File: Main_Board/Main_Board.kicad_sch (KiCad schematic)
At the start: 51 parts, among them J1 RJ45_LED_Shielded, J2 Conn_01x12, SW1 SW_Push, SW2 SW_Push, SW3 SW_Push, SW4 SW_Push, SW5 SW_Push, SW6 SW_Push, SW7 SW_Push, SW8 SW_Push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

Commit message: Overviewed the Board with Drew
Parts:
- added BLUE: D, symbol Device:D
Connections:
- net +3V3: now also BLUE.1 (K); no longer C2.1, C3.1, U1.3 (OUT)
- net GND: no longer U6.5
- new net: BLUE.2 (A), C2.1, C3.1, U1.3 (OUT)
- no-connect marks 62 -> 66
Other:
- moved on the sheet: J2
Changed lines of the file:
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@@
 	)
 	(junction
-		(at 107.95 46.99)
-		(diameter 0)
-		(color 0 0 0 0)
-	)
-	(junction
 		(at 194.31 95.25)
 		(diameter 0)
@@
 	)
 	(junction
+		(at 107.95 46.99)
+		(diameter 0)
+		(color 0 0 0 0)
+	)
+	(junction
 		(at 304.8 171.45)
 		(diameter 0)
@@
 	)
 	(no_connect
+		(at 341.63 34.29)
+	)
+	(no_connect
 		(at 97.79 147.32)
 	)
@@
 	)
 	(no_connect
+		(at 341.63 39.37)
+	)
+	(no_connect
 		(at 341.63 113.03)
 	)
@@
 	)
 	(no_connect
+		(at 341.63 128.27)
+	)
+	(no_connect
 		(at 97.79 157.48)
 	)
@@
 	)
 	(no_connect
+		(at 341.63 36.83)
+	)
+	(no_connect
 		(at 341.63 100.33)
 	)
@@
 	(wire
 		(pts
-			(xy 88.9 127) (xy 83.82 127)
-		)
-		(stroke
-			(width 0)
-			(type default)
-		)
-	)
-	(wire
-		(pts
 			(xy 217.17 195.58) (xy 217.17 186.69)
 		)
@@
 	(wire
 		(pts
-			(xy 107.95 44.45) (xy 107.95 46.99)
-		)
-		(stroke
-			(width 0)
-			(type default)
-		)
-	)
-	(wire
-		(pts
 			(xy 80.01 54.61) (xy 93.98 54.61)
 		)
@@
 	(wire
 		(pts
-			(xy 33.02 93.98) (xy 33.02 101.6)
+			(xy 53.34 99.06) (xy 53.34 101.6)
 		)
 		(stroke
@@
 		)
 	)
-	(wire
-		(pts
-			(xy 33.02 101.6) (xy 53.34 101.6)
-		)
-		(stroke
-			(width 0)
-			(type default)
-		)
-	)
 	(polyline
 		(pts
@@
 		)
 	)
+	(wire
+		(pts
+			(xy 97.79 44.45) (xy 100.33 44.45)
+		)
+		(stroke
+			(width 0)
+			(type default)
+		)
+	)
 	(polyline
 		(pts
@@
 	(wire
 		(pts
+			(xy 97.79 44.45) (xy 97.79 43.18)
+		)
+		(stroke
+			(width 0)
+			(type default)
+		)
+	)
+	(wire
+		(pts
 			(xy 217.17 144.78) (xy 220.98 144.78)
 		)
@@
 		)
 	)
-	(wire
-		(pts
-			(xy 83.82 138.43) (xy 53.34 138.43)
-		)
-		(stroke
-			(width 0)
-			(type default)
-		)
-	)
 	(polyline
 		(pts
@@
 	(wire
 		(pts
-			(xy 83.82 127) (xy 83.82 138.43)
-		)
-		(stroke
-			(width 0)
-			(type default)
-		)
-	)
-	(wire
-		(pts
 			(xy 209.55 60.96) (xy 217.17 60.96)
 		)
@@
 	(wire
 		(pts
+			(xy 107.95 44.45) (xy 107.95 46.99)
+		)
+		(stroke
+			(width 0)
+			(type default)
+		)
+	)
+	(wire
+		(pts
 			(xy 173.99 53.34) (xy 175.26 53.34)
 		)
@@
 	(symbol
 		(lib_id "Connector_Generic:Conn_01x12")
-		(at 610.87 35.56 0)
+		(at 379.73 35.56 0)
 		(unit 1)
 		(exclude_from_sim no)
@@
 		(fields_autoplaced yes)
 		(property "Reference" "J2"
-			(at 613.41 35.5599 0)
+			(at 382.27 35.5599 0)
 			(effects
 				(font
@@
 		)
 		(property "Value" "Conn_01x12"
-			(at 613.41 38.0999 0)
+			(at 382.27 38.0999 0)
 			(effects
 				(font
@@
 		)
 		(property "Footprint" ""
-			(at 610.87 35.56 0)
+			(at 379.73 35.56 0)
 			(effects
 				(font
@@
 		)
 		(property "Datasheet" "~"
-			(at 610.87 35.56 0)
+			(at 379.73 35.56 0)
 			(effects
 				(font
@@
 		)
 		(property "Description" "Generic connector, single row, 01x12, script generated (kicad-library-utils/schlib/autogen/connector/)"
-			(at 610.87 35.56 0)
+			(at 379.73 35.56 0)
 			(effects
 				(font
@@
 	(symbol
 		(lib_id "power:+3.3V")
-		(at 107.95 44.45 0)
+		(at 97.79 43.18 0)
 		(unit 1)
 		(exclude_from_sim no)
@@
 		(dnp no)
 		(property "Reference" "#PWR03"
-			(at 107.95 48.26 0)
+			(at 97.79 46.99 0)
 			(effects
 				(font
@@
 		)
 		(property "Value" "+3V3"
-			(at 104.648 39.624 0)
+			(at 94.488 38.354 0)
 			(effects
 				(font
@@
 		)
 		(property "Footprint" ""
-			(at 107.95 44.45 0)
+			(at 97.79 43.18 0)
 			(effects
 				(font
@@
 		)
 		(property "Datasheet" ""
-			(at 107.95 44.45 0)
+			(at 97.79 43.18 0)
 			(effects
 				(font
@@
 		)
 		(property "Description" "Power symbol creates a global label with name \"+3.3V\""
-			(at 107.95 44.45 0)
+			(at 97.79 43.18 0)
 			(effects
 				(font
@@
 	(symbol
 		(lib_id "power:+3V3")
-		(at 33.02 93.98 0)
+		(at 53.34 99.06 0)
 		(unit 1)
 		(exclude_from_sim no)
@@
 		(fields_autoplaced yes)
 		(property "Reference" "#PWR029"
-			(at 33.02 97.79 0)
+			(at 53.34 102.87 0)
 			(effects
 				(font
@@
 		)
 		(property "Value" "+3V3"
-			(at 33.02 90.4042 0)
+			(at 53.34 95.4842 0)
 			(effects
 				(font
@@
 		)
 		(property "Footprint" ""
-			(at 33.02 93.98 0)
+			(at 53.34 99.06 0)
 			(effects
 				(font
@@
 		)
 		(property "Datasheet" ""
-			(at 33.02 93.98 0)
+			(at 53.34 99.06 0)
 			(effects
 				(font
@@
 		)
 		(property "Description" ""
-			(at 33.02 93.98 0)
+			(at 53.34 99.06 0)
 			(effects
 				(font
@@
 					(unit 1)
 				)
+			)
+		)
+	)
+	(symbol
+		(lib_id "Device:D")
+		(at 104.14 44.45 0)
+		(unit 1)
+		(exclude_from_sim no)
+		(in_bom yes)
+		(on_board yes)
+		(dnp no)
+		(property "Reference" "BLUE"
+			(at 104.14 38.1 0)
+			(effects
+				(font
+					(size 1.27 1.27)
+				)
+			)
+		)
+		(property "Value" "D"
+			(at 104.14 40.64 0)
+			(effects
+				(font
+					(size 1.27 1.27)
+				)
+			)
+		)
+		(property "Footprint" ""
+			(at 104.14 44.45 0)
+			(effects
+				(font
+					(size 1.27 1.27)
+				)
+				(hide yes)
+			)
+		)
+		(property "Datasheet" "~"
+			(at 104.14 44.45 0)
+			(effects
+				(font
+					(size 1.27 1.27)
+				)
+				(hide yes)
+			)
+		)
+		(property "Description" "Diode"
+			(at 104.14 44.45 0)
+			(effects
+				(font
+					(size 1.27 1.27)
+				)
+				(hide yes)
+			)
+		)
+		(property "Sim.Device" "D"
+			(at 104.14 44.45 0)
+			(effects
+				(font
+					(size 1.27 1.27)
+				)
+				(hide yes)
+			)
+		)
+		(property "Sim.Pins" "1=K 2=A"
+			(at 104.14 44.45 0)
+			(effects
+				(font
+					(size 1.27 1.27)
+				)
+				(hide yes)
+			)
+		)
+		(pin "2"
+		)
+		(pin "1"
+		)
+		(instances
+			(project ""
+				(path "/7e76cf6a-e9a4-4ef3-bf05-f0b14a5efcef"
+					(reference "BLUE")
+					(unit 1)
+				)

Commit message: Final edit of the schematic is done
Buttons might change depending on testing results.

Next step:
Test the button system with Drew at the e-lab.
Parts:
- removed BLUE: D, symbol Device:D
- removed D2, D3, D4, D5, D6, D7, D8, D9: BLUE, LED_SMD:LED_0603_1608Metric_Pad1.05x0.95mm_HandSolder, symbol Device:LED
- removed J2: Conn_01x12, symbol Connector_Generic:Conn_01x12
- removed R1, R11, R13, R15: 4.7k, Resistor_SMD:R_0603_1608Metric_Pad0.98x0.95mm_HandSolder, symbol Device:R
- removed R10, R12, R14, R16: 120, Resistor_SMD:R_0603_1608Metric_Pad0.98x0.95mm_HandSolder, symbol Device:R
- removed SNx4HC1: ~, Package_SO:SO-14_5.3x10.2mm_P1.27mm, symbol MRDT_ICs:SNx4HC00
- removed SW1: SW_Push, Button_Switch_SMD:SW_SPST_TL3305A, symbol Switch:SW_Push
- removed U3: AS5048A, Package_SO:TSSOP-14_4.4x5mm_P0.65mm, symbol Sensor_Magnetic:AS5048A
- removed U4: 74HC148, Package_SO:SOIC-16_4.55x10.3mm_P1.27mm, symbol 74xx:74LS148
- removed U6: 74HC00, Package_SO:SO-14_5.3x10.2mm_P1.27mm, symbol 74xx:74HC00
- added SW9: SW_Push, Button_Switch_SMD:SW_SPST_TL3305A, symbol Switch:SW_Push
- R2, R4, R6, R8: value 120 -> 20; footprint Resistor_SMD:R_0603_1608Metric_Pad0.98x0.95mm_HandSolder -> (none)
- R3, R5, R7, R9: value 4.7k -> 20; footprint Resistor_SMD:R_0603_1608Metric_Pad0.98x0.95mm_HandSolder -> (none)
- renumbered R17 to R1, SW9 to SW1
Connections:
- net B1 is gone; now on net +3.3V: R2.1
- net B6 is gone; now on net OUT0: SW6.2
- net B7 is gone; now on net OUT0: SW7.2
- net B8 is gone; now on net OUT0: SW8.2
- net +3V3: now also D1.1 (K); no longer D1.2 (A), R3.1, R5.1, R7.1, R9.1
- net GND: now also R1.1, R9.2, SW9.1; no longer SW2.1, SW3.1, SW4.1, SW5.1, SW6.1, SW7.1, SW8.1
- net J1RX: now also Conn2.1
- net J1TX: now also Conn2.2
- net J2RX: now also Conn2.4; no longer Conn2.1
- net J2TX: now also Conn2.5; no longer Conn2.2
- net J3RX: now also Conn2.7; no longer Conn2.4
- net J3TX: now also Conn2.8; no longer Conn2.5
- net J4RX: now also Conn1.1; no longer Conn2.7
- net J4TX: now also Conn1.2; no longer Conn2.8
- net J5RX: now also Conn1.4; no longer Conn1.1
- net J5TX: now also Conn1.5; no longer Conn1.2
- net J6RX: now also Conn1.7; no longer Conn1.4
- net J6TX: now also Conn1.8; no longer Conn1.5
- net OUT0: now also SW2.2, SW3.2, SW4.2, SW5.2, SW9.2
- net at R6.2: now also R7.1, SW6.1
- net at C2.1, C3.1, U1.3 (OUT): now also D1.2 (A)
- net at R2.2: now also R3.1, SW2.1; no longer D1.1 (K)
- net at R8.2: now also R9.1, SW8.1
- net at R4.2: now also R5.1, SW4.1
- net +5V: no longer names the net of U2.5V
- net B2: no longer names the net of R3.2, R4.1
- net B2: now also SW3.1; no longer SW2.2
- net B3: no longer names the net of R5.2, R6.1
- net B3: now also SW5.1; no longer SW3.2
- net B4: no longer names the net of R7.2, R8.1
- net B4: now also SW7.1; no longer SW4.2
- removed net B5: R9.2, SW5.2
- net J7RX: no longer names the net of U2.34 (RX8)
- net J7RX: no longer Conn1.7
- net J7TX: no longer names the net of U2.35 (TX8)
- net J7TX: no longer Conn1.8
- net OUT1: no longer names the net of U2.19 (A5)
- no-connect marks 66 -> 40
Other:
- note added: "36v-7v to 3.3v Buck Converter"
- note added: "Andersons"
- note added: "Buttons"
- note added: "Connectors (UART)"
- note added: "Ethernet (I/O)"
- note added: "Power"
- note added: "Reverse Switch"
- note added: "Teensy (Micro-controller)"
- note removed: "Encoders"
- moved on the sheet: 100nf, C1, C2, C3, C4, Conn1, Conn2, Conn3A, Conn3B, J1, R1, SW1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

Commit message: Changed the name of the board
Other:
- title: Brushless Arm Tester Board -> Brushless Arm Board
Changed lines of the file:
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@@
 	(paper "User" 266.7 203.2)
 	(title_block
-		(title "Brushless Arm Tester Board")
+		(title "Brushless Arm Board")
 		(date "2024-10-19")
 		(rev "1")

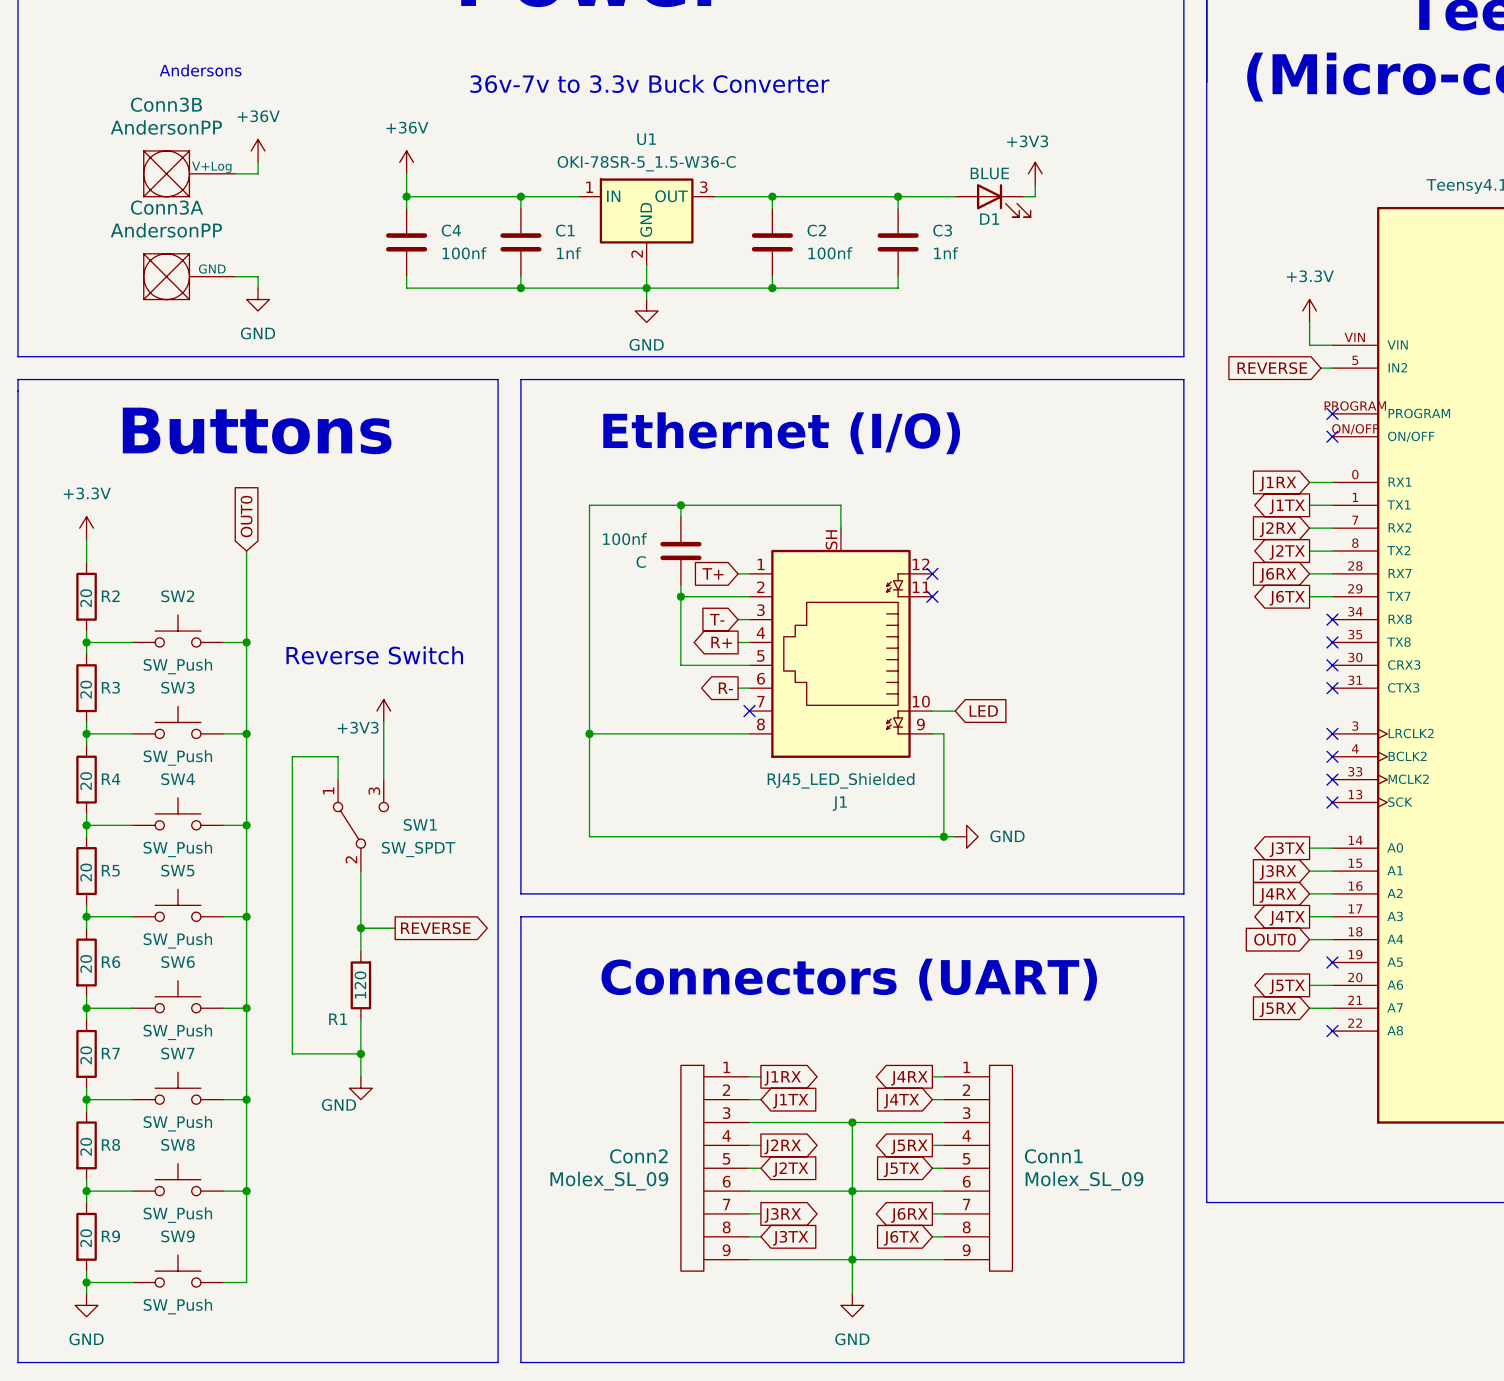
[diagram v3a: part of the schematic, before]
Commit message: Fixed some CDR complaints
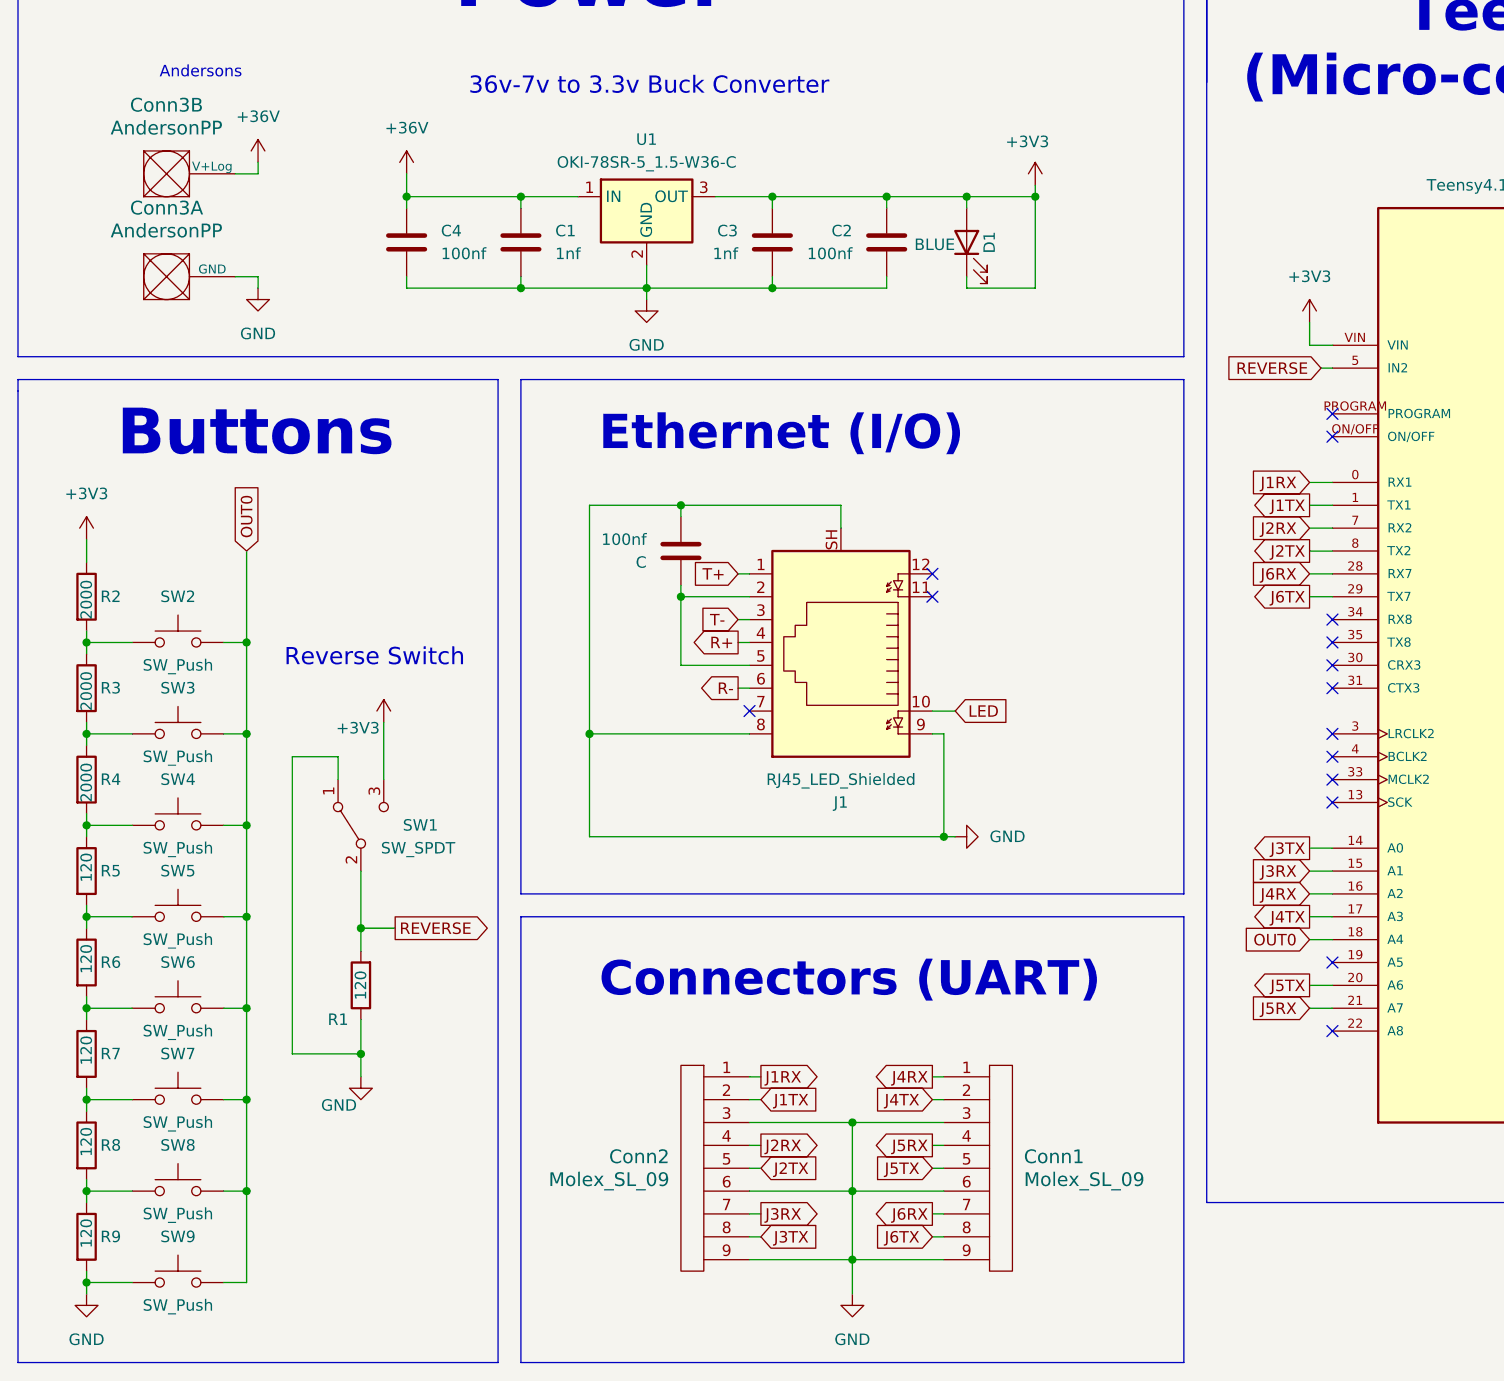
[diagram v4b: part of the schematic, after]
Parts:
- R2, R3, R4: value 20 -> 2000
- R5, R6, R7, R8, R9: value 20 -> 120
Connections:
- net +3.3V is gone; now on net +3V3: R2.1, U2.VIN
- net +3V3: now also C2.1, C3.1, D1.2 (A), U1.3 (OUT)
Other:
- moved on the sheet: C2, C3, D1
